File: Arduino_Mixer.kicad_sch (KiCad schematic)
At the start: 7 parts

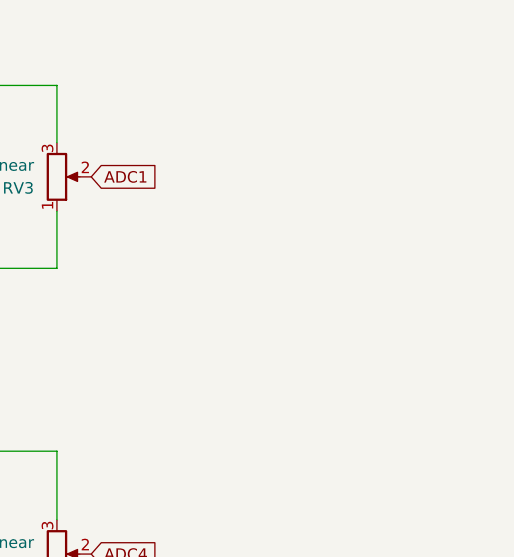
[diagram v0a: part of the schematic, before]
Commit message: Added 4 corner and 1 mid mounting hole for PCB. Generated 3D model output to use when creating 3D printed spacer (using Freecad and KiCadStepUp plugin)
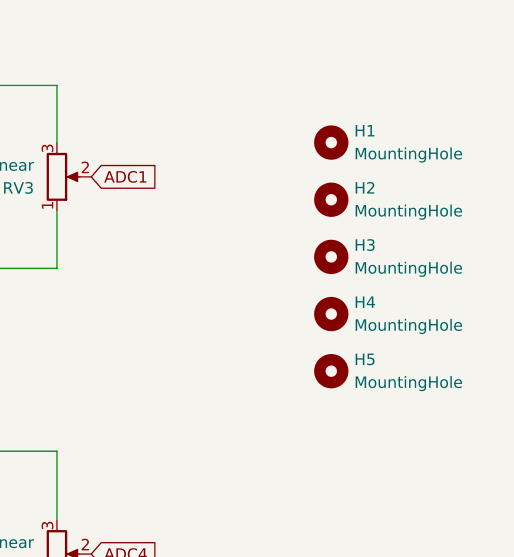
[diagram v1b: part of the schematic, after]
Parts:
- added H1, H2, H3, H4, H5: MountingHole, MountingHole:MountingHole_3.2mm_M3_ISO14580, symbol Mechanical:MountingHole

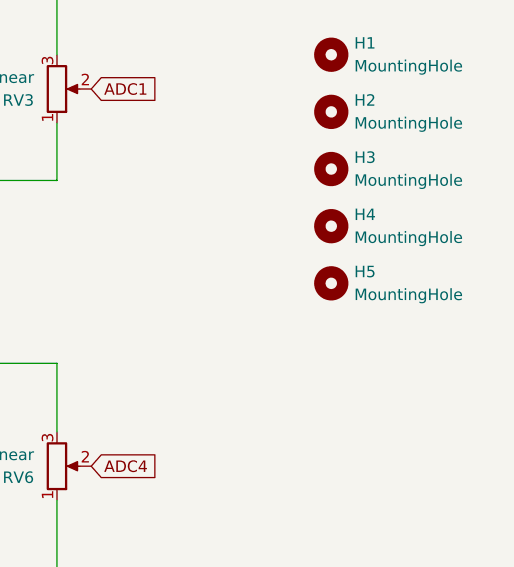
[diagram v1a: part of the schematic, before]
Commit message: Removed central hole as assymetry would not have worked with assembled PCB when flipped
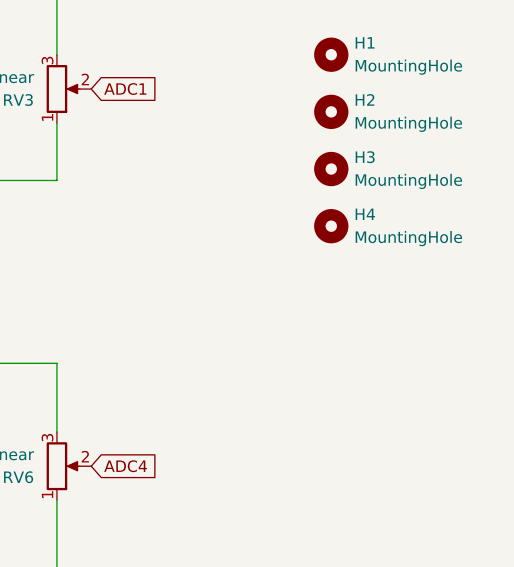
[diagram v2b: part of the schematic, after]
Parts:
- removed H5: MountingHole, MountingHole:MountingHole_3.2mm_M3_ISO14580, symbol Mechanical:MountingHole
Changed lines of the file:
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@@
-	)
-	(symbol
-		(lib_id "Mechanical:MountingHole")
-		(at 236.22 77.47 0)
-		(unit 1)
-		(exclude_from_sim no)
-		(in_bom yes)
-		(on_board yes)
-		(dnp no)
-		(fields_autoplaced yes)
-		(property "Reference" "H5"
-			(at 238.76 76.1999 0)
-			(effects
-				(font
-					(size 1.27 1.27)
-				)
-				(justify left)
-			)
-		)
-		(property "Value" "MountingHole"
-			(at 238.76 78.7399 0)
-			(effects
-				(font
-					(size 1.27 1.27)
-				)
-				(justify left)
-			)
-		)
-		(property "Footprint" "MountingHole:MountingHole_3.2mm_M3_ISO14580"
-			(at 236.22 77.47 0)
-			(effects
-				(font
-					(size 1.27 1.27)
-				)
-				(hide yes)
-			)
-		)
-		(property "Datasheet" "~"
-			(at 236.22 77.47 0)
-			(effects
-				(font
-					(size 1.27 1.27)
-				)
-				(hide yes)
-			)
-		)
-		(property "Description" "Mounting Hole without connection"
-			(at 236.22 77.47 0)
-			(effects
-				(font
-					(size 1.27 1.27)
-				)
-				(hide yes)
-			)
-		)
-		(instances
-			(project "Arduino_Mixer"
-				(path "/37fed42c-5669-4ade-a8bd-0146a07809af"
-					(reference "H5")
-					(unit 1)
-				)
-			)
-		)
 	)
 	(symbol

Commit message: First release candidate Added alw Audio logo, produced gerber plots using JLPCB guidelines: https://jlcpcb.com/help/article/362-how-to-generate-gerber-and-drill-files-in-kicad-8
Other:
- company: (none) -> alw Audio
- title: (none) -> Arduino nano hardware mixer controls for deej project
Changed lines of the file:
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@@
 	(generator_version "8.0")
 	(paper "A4")
+	(title_block
+		(title "Arduino nano hardware mixer controls for deej project")
+		(date "2024-03-31")
+		(rev "1.0")
+		(company "alw Audio")
+		(comment 1 "PCB idea based on https://github.com/Snackya/Snackboard-mix project")
+		(comment 2 "corresponding cross-platform PC application,")
+		(comment 3 "Arduino Nano hardware mixer control PCB design for use with deej project and ")
+	)
 	(junction
 		(at 182.88 110.49)
